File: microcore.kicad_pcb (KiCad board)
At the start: 4 copper layers, 90 x 60 mm, 21 parts, among them J1 TE_776231-1, J8 USB_B_Mini, M1 Module:mega-mcu100/0.3, M2 Module-power_12and5V-0.3, M3 Module-vr-max9924-0.3, Q1 VND14NV04-E, Q2 VND14NV04-E, Q3 VND14NV04-E, Q4 VND14NV04-E, Q5 VND14NV04-E, Q6 VND14NV04-E, Q7 VND14NV04-E

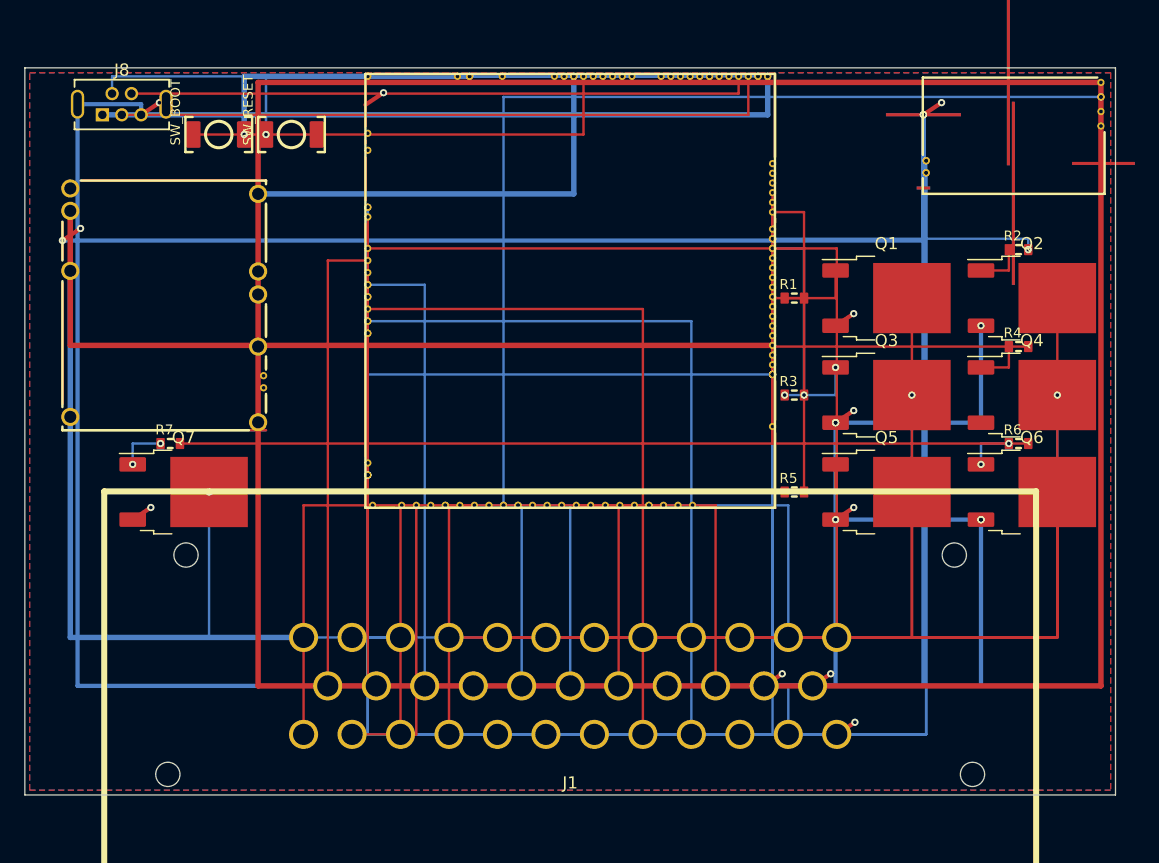
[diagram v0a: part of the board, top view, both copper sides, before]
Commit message: Fix Create Board: drop GND zones that break gerbmerge trim
gerbmerge rectCenter crashes on float extents from zone polygons
(TypeError: float & int). Keep scripted frame tracks/vias; pours later.
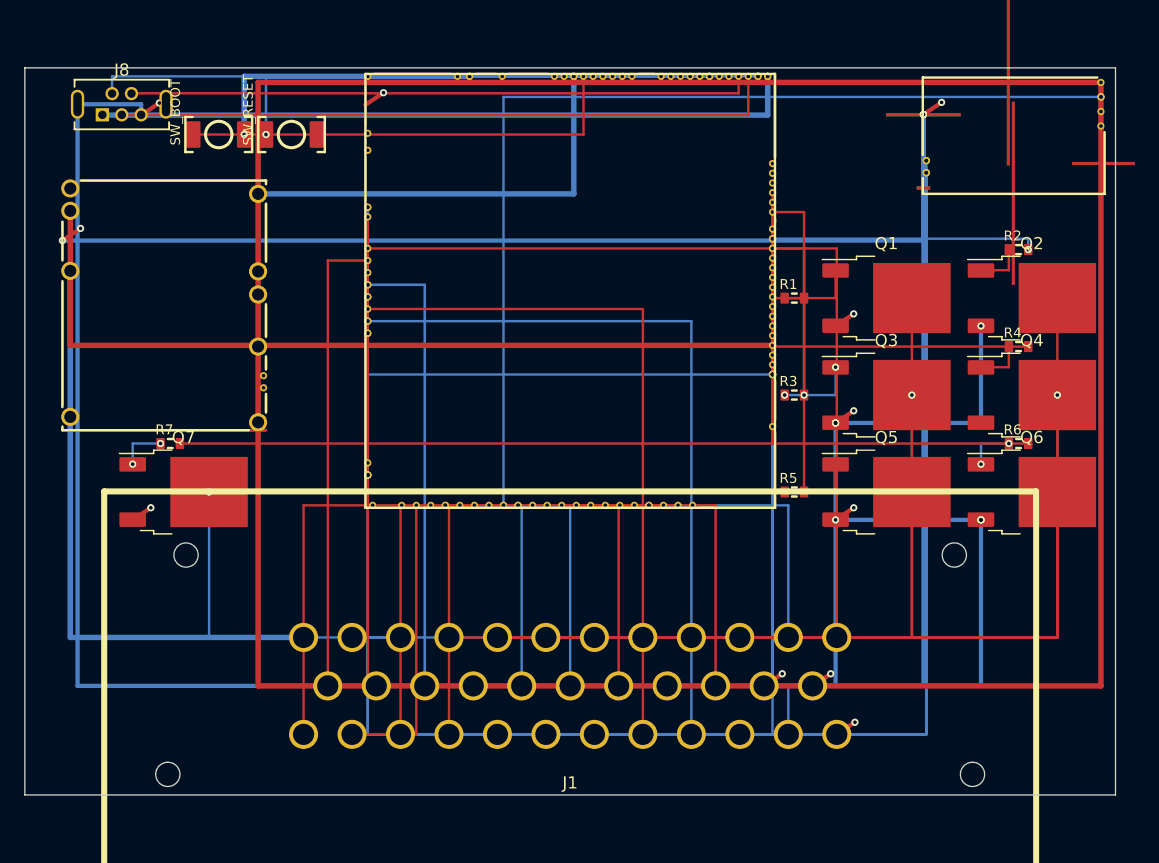
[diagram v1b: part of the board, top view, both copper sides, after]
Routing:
- removed copper zone on B.Cu, net GND
- removed copper zone on F.Cu, net GND

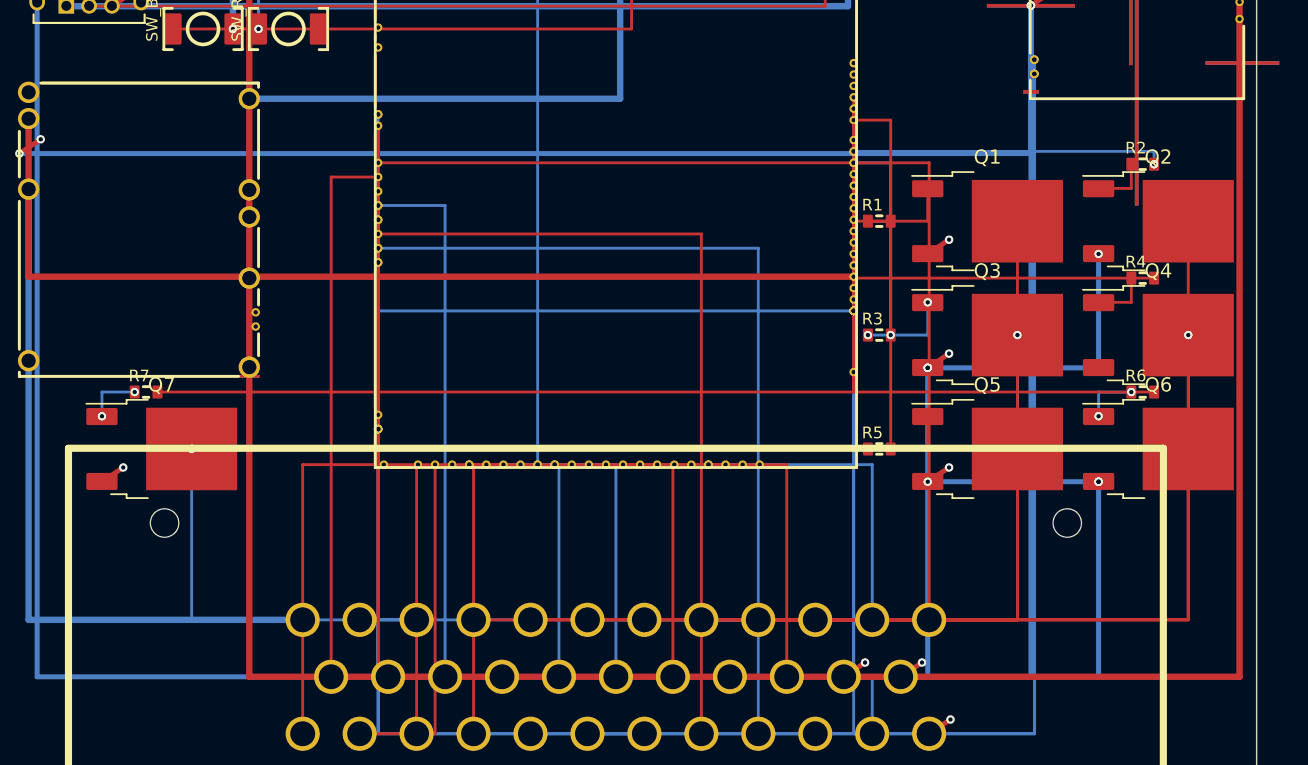
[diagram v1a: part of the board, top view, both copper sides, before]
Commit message: Rev f: clear AMPSEAL silk keepout for DPAKs
Re-nest Q1–Q6 to y=15/22/29 (left x=68, right x=82) with gate Rs
clear of drain pads; move Q7+R7 into M2–M1 corridor (Q7 rot 90);
jog IGN2 around Q7; rebuild FET tracks/vias. Nothing in J1 silk
keepout (y≥35). Bump BOARD_REVISION to f.
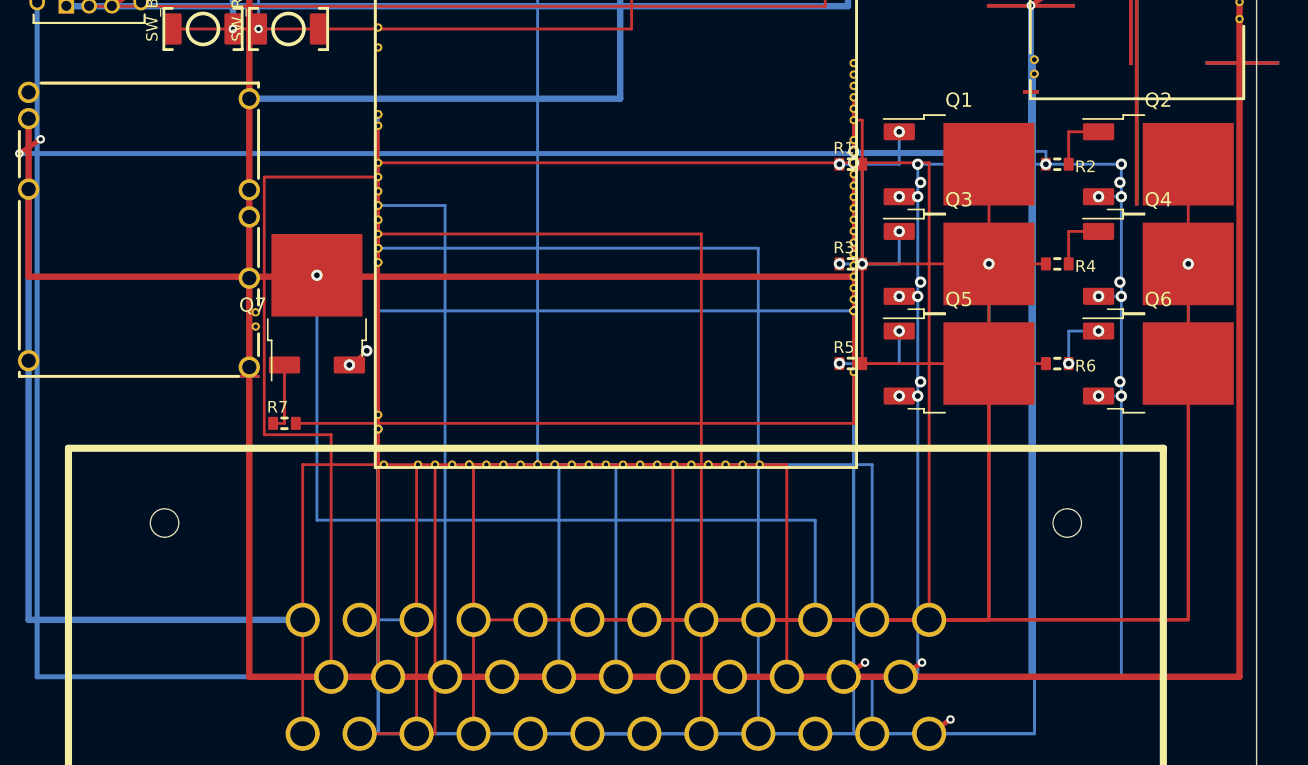
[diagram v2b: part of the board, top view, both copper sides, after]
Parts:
- moved Q7 15.0 mm to (24.0, 26.0), turned to 90 degrees
- moved R7 9.97 mm to (21.7, 33.2)
- moved Q5 6.32 mm to (68.0, 29.0)
- moved R5 6.32 mm to (61.5, 29.0)
- moved R6 6.32 mm to (76.0, 29.0), turned to 180 degrees
- moved R4 6.08 mm to (76.0, 22.0), turned to 180 degrees
- moved Q6 6.00 mm to (82.0, 29.0)
- moved R2 6.00 mm to (76.0, 15.0), turned to 180 degrees
- moved Q3 5.39 mm to (68.0, 22.0)
- moved R3 5.39 mm to (61.5, 22.0)
- moved Q4 5.00 mm to (82.0, 22.0)
- moved Q1 4.47 mm to (68.0, 15.0)
- moved R1 4.47 mm to (61.5, 15.0)
- moved Q2 4.00 mm to (82.0, 15.0)
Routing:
- net /OUT_LS2: track 41.0 -> 31.4 mm
- net /IGN2: track 38.4 -> 47.8 mm
- net /OUT_INJ4: track 28.4 -> 19.8 mm
- net /OUT_LS1: track 25.7 -> 17.7 mm
- net /OUT_INJ2: track 22.0 -> 14.4 mm
- net /OUT_LS3: track 69.6 -> 62.1 mm
- net /OUT_INJ3: track 14.7 -> 7.70 mm
- net /OUT_INJ1: track 8.30 -> 2.30 mm
- net /LS2_IDLE: track 42.2 -> 48.2 mm
- net GND: track 367.6 -> 372.8 mm, vias 29 -> 41
- net /INJ4: track 58.2 -> 63.2 mm
- net /LS1_FP: track 34.2 -> 38.2 mm
- net /INJ2: track 74.2 -> 78.2 mm
- net /LS3_BOOST: track 55.8 -> 59.2 mm
- net /INJ3: track 50.2 -> 53.2 mm
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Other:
- board text added: "Micro Core rev F 90x60 4-layer mega-mcu100/0.3 + power + vr-max9924/0.3 USB Mini-B + SW_BOOT/SW_RESET north + TE 776231-1 south"
- board text removed: "Micro Core rev D 90x60 4-layer mega-mcu100/0.3 + power + vr-max9924/0.3 USB Mini-B + SW_BOOT/SW_RESET north + TE 776231-1 south"

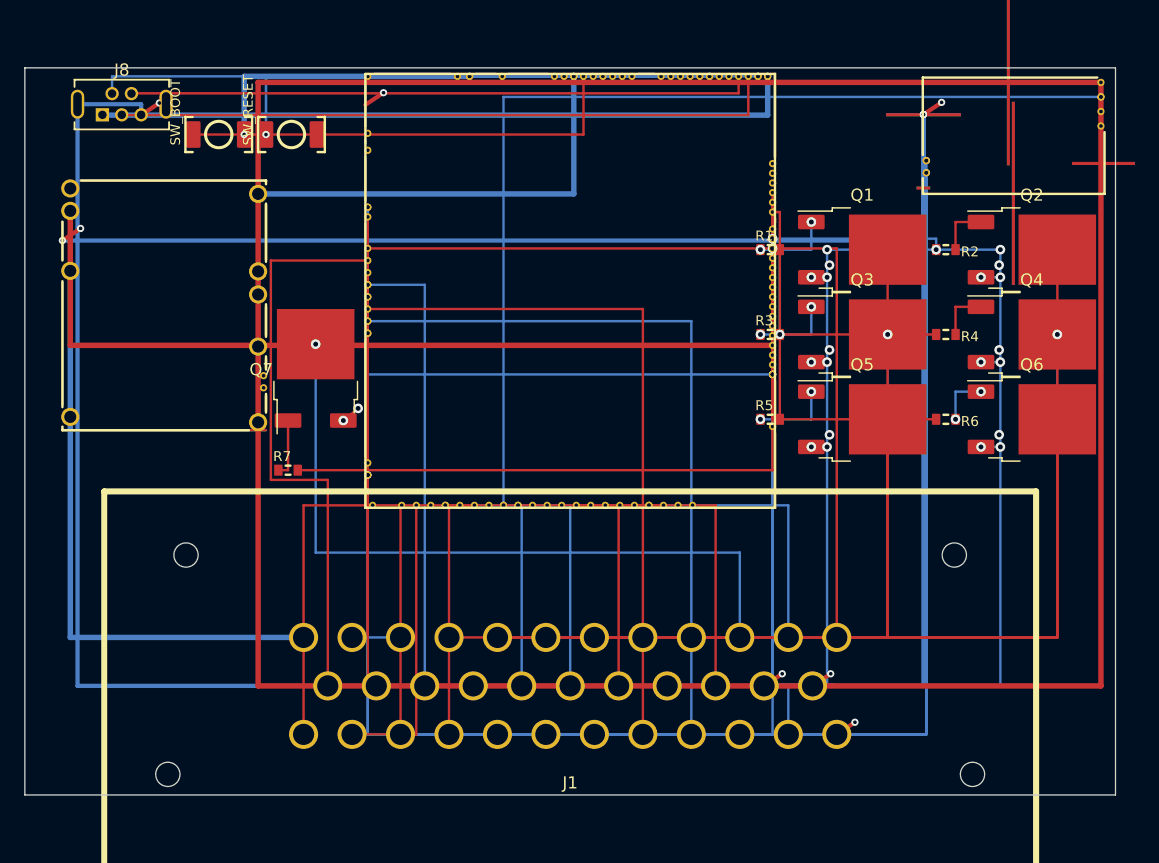
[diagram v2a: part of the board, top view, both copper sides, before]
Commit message: Rev g: add F.Cu and B.Cu GND copper pours
Board-interior GND zones (0.4 mm inset, clearance 0.2, thermal
0.25/0.3) on F.Cu and B.Cu only; filled via pcbnew. SGND left
separate. AMPSEAL keepout positions unchanged. ASCII bom_replace-g.
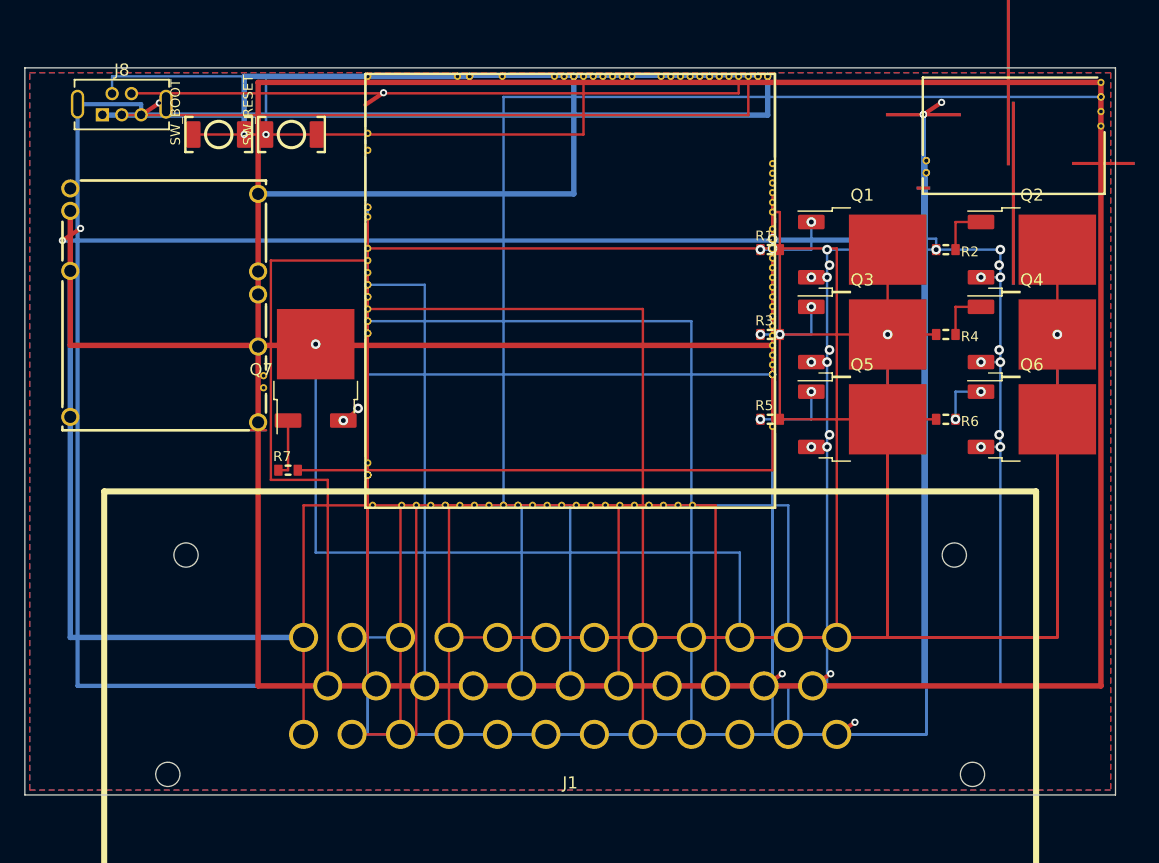
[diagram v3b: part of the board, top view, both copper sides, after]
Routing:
- added copper zone on B.Cu, net GND
- added copper zone on F.Cu, net GND
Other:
- board text added: "Micro Core rev G 90x60 4-layer mega-mcu100/0.3 + power + vr-max9924/0.3 USB Mini-B + SW_BOOT/SW_RESET north + TE 776231-1 south"
- board text removed: "Micro Core rev F 90x60 4-layer mega-mcu100/0.3 + power + vr-max9924/0.3 USB Mini-B + SW_BOOT/SW_RESET north + TE 776231-1 south"

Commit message: Add files via upload
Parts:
- moved Q7 185.6 mm to (189.6, 109.8), turned to 0 degrees
- moved R7 179.8 mm to (184.2, 110.3), turned to -90 degrees
- moved J1 133.2 mm to (152.2, 130.0)
- moved R5 132.7 mm to (171.8, 102.7)
- moved R3 132.0 mm to (171.8, 94.5)
- moved R1 131.4 mm to (171.8, 86.5), turned to 180 degrees
- moved R6 131.2 mm to (185.5, 101.3)
- moved R2 130.8 mm to (185.5, 86.5)
- moved R4 130.8 mm to (185.5, 93.5)
- moved Q5 130.4 mm to (175.5, 102.7)
- moved Q3 129.7 mm to (175.5, 94.5)
- moved Q6 129.6 mm to (189.5, 101.3)
- moved J8 129.5 mm to (114.9, 76.1)
- moved M2 129.3 mm to (109.8, 102.9)
- moved Q1 129.1 mm to (175.5, 86.5)
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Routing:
- net GND: track 372.8 -> 10.6 mm, vias 41 -> 6
- net /V5_REF: track 238.7 -> 161.4 mm, vias 0 -> 4
- net /SGND: track 163.2 -> 101.9 mm, vias 10 -> 2
- net /VIGN_SENSE: track 69.0 -> 100.6 mm, vias 0 -> 2
- net /IGN5: track 54.8 -> 84.8 mm, vias 2 -> 3
- net /LS3_BOOST: track 59.2 -> 33.5 mm, vias 2 -> 0
- net /OUT_LS3: track 62.1 -> 38.6 mm, vias 0 -> 1
- net /IGN8: track 63.8 -> 83.3 mm
- net /VR_P: track 81.8 -> 100.5 mm
- net /IGN3: track 34.8 -> 47.0 mm, vias 0 -> 2
- net /CAN_L: track 38.2 -> 50.1 mm
- net /INJ2: track 78.2 -> 67.0 mm, vias 0 -> 3
- net /IGN1: track 70.8 -> 81.0 mm
- net /CAN_H: track 36.0 -> 46.1 mm
- net /VR_OUT: track 83.0 -> 74.3 mm, vias 2 -> 4
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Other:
- board size 90 x 60 mm -> 90 x 76.6 mm

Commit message: Fix drill origin to Edge.Cuts bottom-left so create-board HTML BOM can parse rev h
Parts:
- removed J1: TE_776231-1, kicad6-libraries:TE_776231
- removed J8: USB_B_Mini, hellen-one-common:USB-MINI-B-VERTICAL
- removed M1: Module:mega-mcu100/0.3, hellen-one-mega-mcu100-0.3:mega-mcu100
- removed M2: Module-power_12and5V-0.3, hellen-one-power_12and5V-0.3:power_12and5V
- removed M3: Module-vr-max9924-0.3, hellen-one-vr-max9924-0.3:vr-max9924
- removed Q1, Q2, Q3, Q4, Q5, Q6, Q7: VND14NV04-E, DPAK
- removed R1, R2, R3, R4, R5, R6, R7: 12, R0603
- removed SW_BOOT, SW_RESET: BTN, hellen-one-common:SMD-2_2.9x3.9x1.7
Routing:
- net /V5_REF: track 161.4 -> 0.00 mm, vias 4 -> 0
- net /SGND: track 101.9 -> 0.00 mm, vias 2 -> 0
- net /VIGN_SENSE: track 100.6 -> 0.00 mm, vias 2 -> 0
- net /VR_P: track 100.5 -> 0.00 mm, vias 2 -> 0
- net /VR_N: track 85.5 -> 0.00 mm, vias 3 -> 0
- net /IGN5: track 84.8 -> 0.00 mm, vias 3 -> 0
- net /IGN8: track 83.3 -> 0.00 mm, vias 2 -> 0
- net /IGN1: track 81.0 -> 0.00 mm
- net /VR_OUT: track 74.3 -> 0.00 mm, vias 4 -> 0
- net /INJ2: track 67.0 -> 0.00 mm, vias 3 -> 0
- net /IGN7: track 61.8 -> 0.00 mm, vias 2 -> 0
- net /INJ1: track 60.4 -> 0.00 mm, vias 2 -> 0
- net /VBUS: track 58.1 -> 0.00 mm, vias 4 -> 0
- net /IGN6: track 56.4 -> 0.00 mm
- net /INJ4: track 54.8 -> 0.00 mm, vias 3 -> 0
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- removed copper zone on B.Cu, net GND
- removed copper zone on F.Cu, net GND
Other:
- board outline removed
- copper layers 4 -> 0
- board text removed: "Micro Core rev G 90x60 4-layer mega-mcu100/0.3 + power + vr-max9924/0.3 USB Mini-B + SW_BOOT/SW_RESET north + TE 776231-1 south"

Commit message: Restore microcore.kicad_pcb and set drill origin to Edge.Cuts bottom-left (rev h)
ce63db4 wiped the PCB to ~49 bytes; restore from 298ebd5 and set
aux/grid origin to Edge.Cuts BL (107.5, 148.0872). Add empty-PCB guard.
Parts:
- added J1: TE_776231-1, kicad6-libraries:TE_776231, F.Cu at (152.2, 130.0)
- added J8: USB_B_Mini, hellen-one-common:USB-MINI-B-VERTICAL, F.Cu at (114.9, 76.1)
- added M1: Module:mega-mcu100/0.3, hellen-one-mega-mcu100-0.3:mega-mcu100, F.Cu at (133.2, 110.0)
- added M2: Module-power_12and5V-0.3, hellen-one-power_12and5V-0.3:power_12and5V, F.Cu at (109.8, 102.9)
- added M3: Module-vr-max9924-0.3, hellen-one-vr-max9924-0.3:vr-max9924, F.Cu at (178.6, 82.3)
- added Q1: VND14NV04-E, DPAK, F.Cu at (175.5, 86.5)
- added Q2: VND14NV04-E, DPAK, F.Cu at (189.5, 86.5)
- added Q3: VND14NV04-E, DPAK, F.Cu at (175.5, 94.5)
- added Q4: VND14NV04-E, DPAK, F.Cu at (189.5, 93.5)
- added Q5: VND14NV04-E, DPAK, F.Cu at (175.5, 102.7)
- added Q6: VND14NV04-E, DPAK, F.Cu at (189.5, 101.3)
- added Q7: VND14NV04-E, DPAK, F.Cu at (189.6, 109.8)
- added R1: 12, R0603, F.Cu at (171.8, 86.5)
- added R2: 12, R0603, F.Cu at (185.5, 86.5)
- added R3: 12, R0603, F.Cu at (171.8, 94.5)
- added R4: 12, R0603, F.Cu at (185.5, 93.5)
- added R5: 12, R0603, F.Cu at (171.8, 102.7)
- added R6: 12, R0603, F.Cu at (185.5, 101.3)
- added R7: 12, R0603, F.Cu at (184.2, 110.3)
- added SW_BOOT: BTN, hellen-one-common:SMD-2_2.9x3.9x1.7, F.Cu at (123.5, 77.0)
- added SW_RESET: BTN, hellen-one-common:SMD-2_2.9x3.9x1.7, F.Cu at (127.5, 76.9)
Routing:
- net /V5_REF: track 0.00 -> 161.4 mm, vias 0 -> 4
- net /SGND: track 0.00 -> 101.9 mm, vias 0 -> 2
- net /VIGN_SENSE: track 0.00 -> 100.6 mm, vias 0 -> 2
- net /VR_P: track 0.00 -> 100.5 mm, vias 0 -> 2
- net /VR_N: track 0.00 -> 85.5 mm, vias 0 -> 3
- net /IGN5: track 0.00 -> 84.8 mm, vias 0 -> 3
- net /IGN8: track 0.00 -> 83.3 mm, vias 0 -> 2
- net /IGN1: track 0.00 -> 81.0 mm
- net /VR_OUT: track 0.00 -> 74.3 mm, vias 0 -> 4
- net /INJ2: track 0.00 -> 67.0 mm, vias 0 -> 3
- net /IGN7: track 0.00 -> 61.8 mm, vias 0 -> 2
- net /INJ1: track 0.00 -> 60.4 mm, vias 0 -> 2
- net /VBUS: track 0.00 -> 58.1 mm, vias 0 -> 4
- net /IGN6: track 0.00 -> 56.4 mm
- net /INJ4: track 0.00 -> 54.8 mm, vias 0 -> 3
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- added copper zone on B.Cu, net GND
- added copper zone on F.Cu, net GND
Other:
- board outline added: 90 x 76.6 mm
- copper layers 0 -> 4
- board text added: "Micro Core rev G 90x60 4-layer mega-mcu100/0.3 + power + vr-max9924/0.3 USB Mini-B + SW_BOOT/SW_RESET north + TE 776231-1 south"

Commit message: Rev i: J8 GND stitch, FET/gate LCSC, rev-h status (not fab-ready)
Stitch J8 pads 5/6 to new GND via (clear of VBUS). Assign C155647/C22783
in bom_replace. Waive frame ANALOG/HALL to mega-module input lite. Document
KiCad 10 DRC vs rev-g and flyback/TVS layout blocker for Boss.
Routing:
- net GND: track 10.6 -> 25.6 mm, vias 6 -> 7
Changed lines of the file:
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@@
+	)
+	(via
+		(at 114.9 79.5)
+		(size 0.8)
+		(drill 0.4)
+		(layers "F.Cu" "B.Cu")
+		(net "GND")
+	)
+	(segment
+		(start 111.25 76.125)
+		(end 111.25 79.5)
+		(width 0.4)
+		(layer "F.Cu")
+		(net "GND")
+	)
+	(segment
+		(start 111.25 79.5)
+		(end 114.9 79.5)
+		(width 0.4)
+		(layer "F.Cu")
+		(net "GND")
+	)
+	(segment
+		(start 116.5 77)
+		(end 114.9 79.5)
+		(width 0.4)
+		(layer "F.Cu")
+		(net "GND")
+	)
+	(segment
+		(start 118.55 76.125)
+		(end 114.9 79.5)
+		(width 0.4)
+		(layer "F.Cu")
+		(net "GND")
 	)
 	(via
